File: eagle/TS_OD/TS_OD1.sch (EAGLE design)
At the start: 44 parts, among them IC1 LM4558N, T1 2SC1815, T2 2SC1814

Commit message: change eagle files' name from TS_OD to TS_OD1
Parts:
- C10, C11: device rcl:CPOL-EUE2.5-7 -> rcl:CPOL-EUE5-6
- R7: device rcl:R-EU_0207/7 -> rcl:R-EU_0207/10
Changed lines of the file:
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@@
 <part name="P+4" library="supply1" deviceset="VCC/2" device=""/>
 <part name="JP2" library="pinhead" deviceset="PINHD-1X2" device="" value="DRIVE"/>
-<part name="R7" library="rcl" deviceset="R-EU_" device="0207/7" value="1k"/>
+<part name="R7" library="rcl" deviceset="R-EU_" device="0207/10" value="1k"/>
 <part name="R9" library="rcl" deviceset="R-EU_" device="0207/7" value="10k"/>
 <part name="C5" library="rcl" deviceset="C-EU" device="050-035X075" value="0.22uF"/>
@@
 <part name="R16" library="rcl" deviceset="R-EU_" device="0207/7" value="10k"/>
 <part name="R17" library="rcl" deviceset="R-EU_" device="0207/7" value="10k"/>
-<part name="C10" library="rcl" deviceset="CPOL-EU" device="E2.5-7" value="100uF"/>
-<part name="C11" library="rcl" deviceset="CPOL-EU" device="E2.5-7" value="47uF"/>
+<part name="C10" library="rcl" deviceset="CPOL-EU" device="E5-6" value="100uF"/>
+<part name="C11" library="rcl" deviceset="CPOL-EU" device="E5-6" value="47uF"/>
 <part name="GND9" library="supply1" deviceset="GND" device=""/>
 <part name="P+9" library="supply1" deviceset="VCC/2" device=""/>

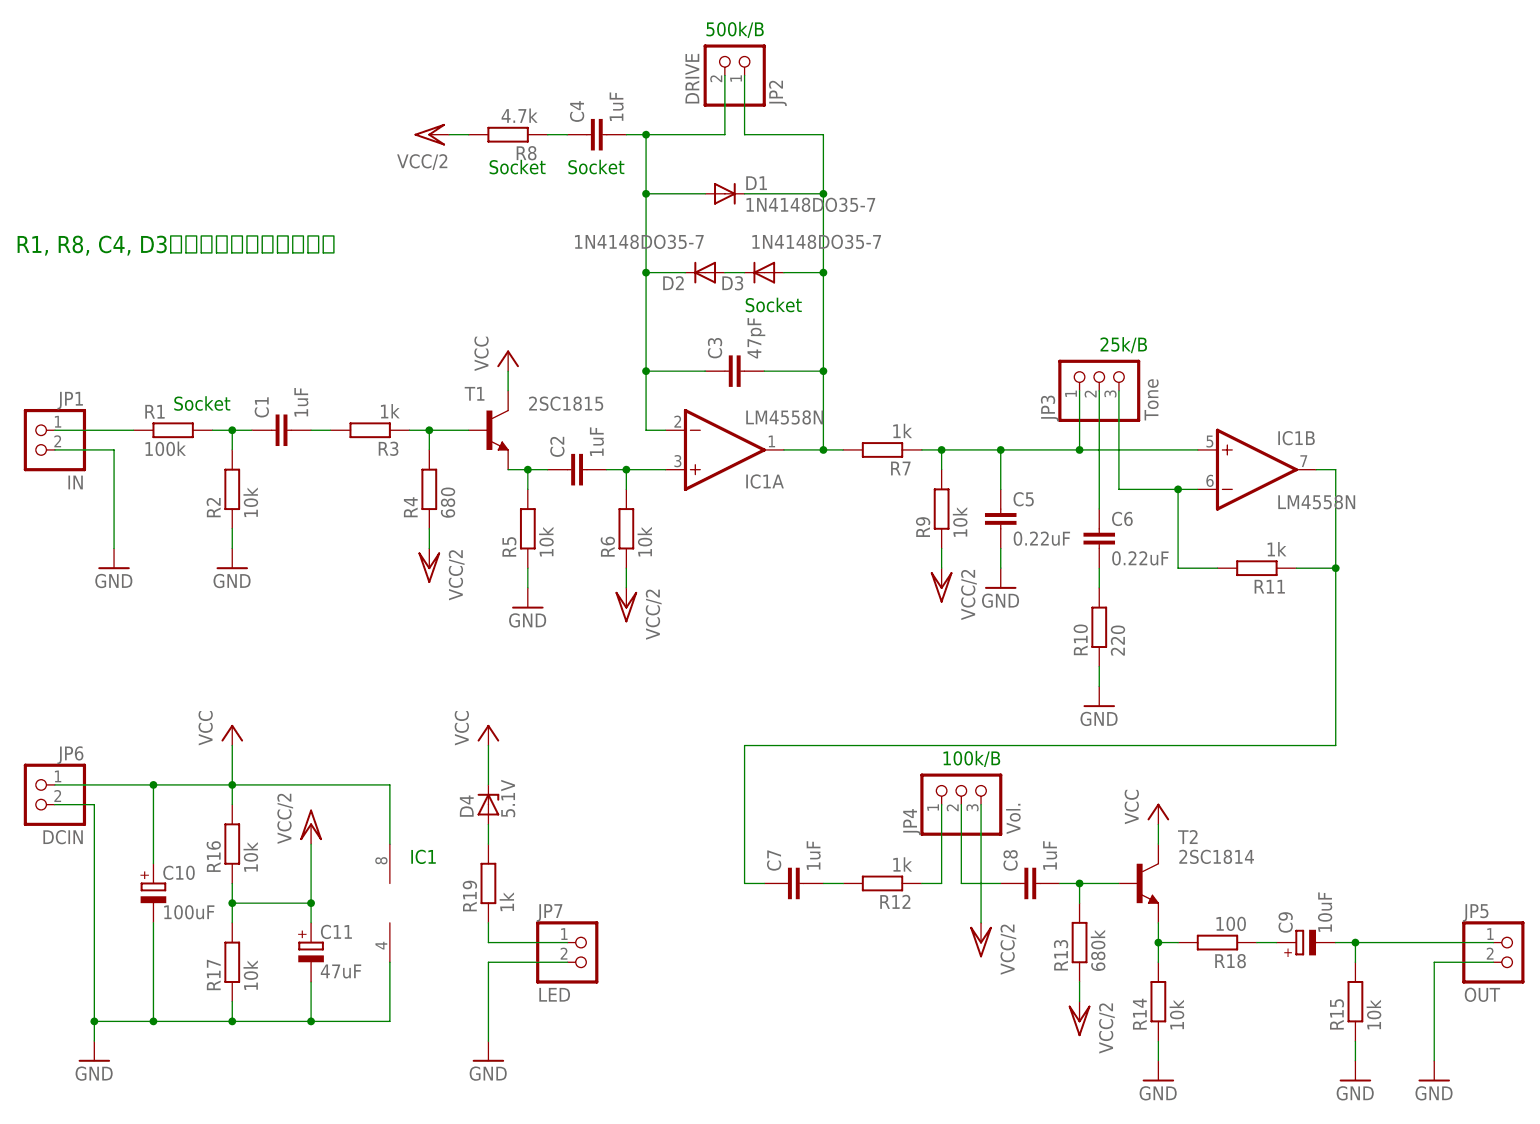
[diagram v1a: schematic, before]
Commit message: Update: eagle files Add: drawing of the case
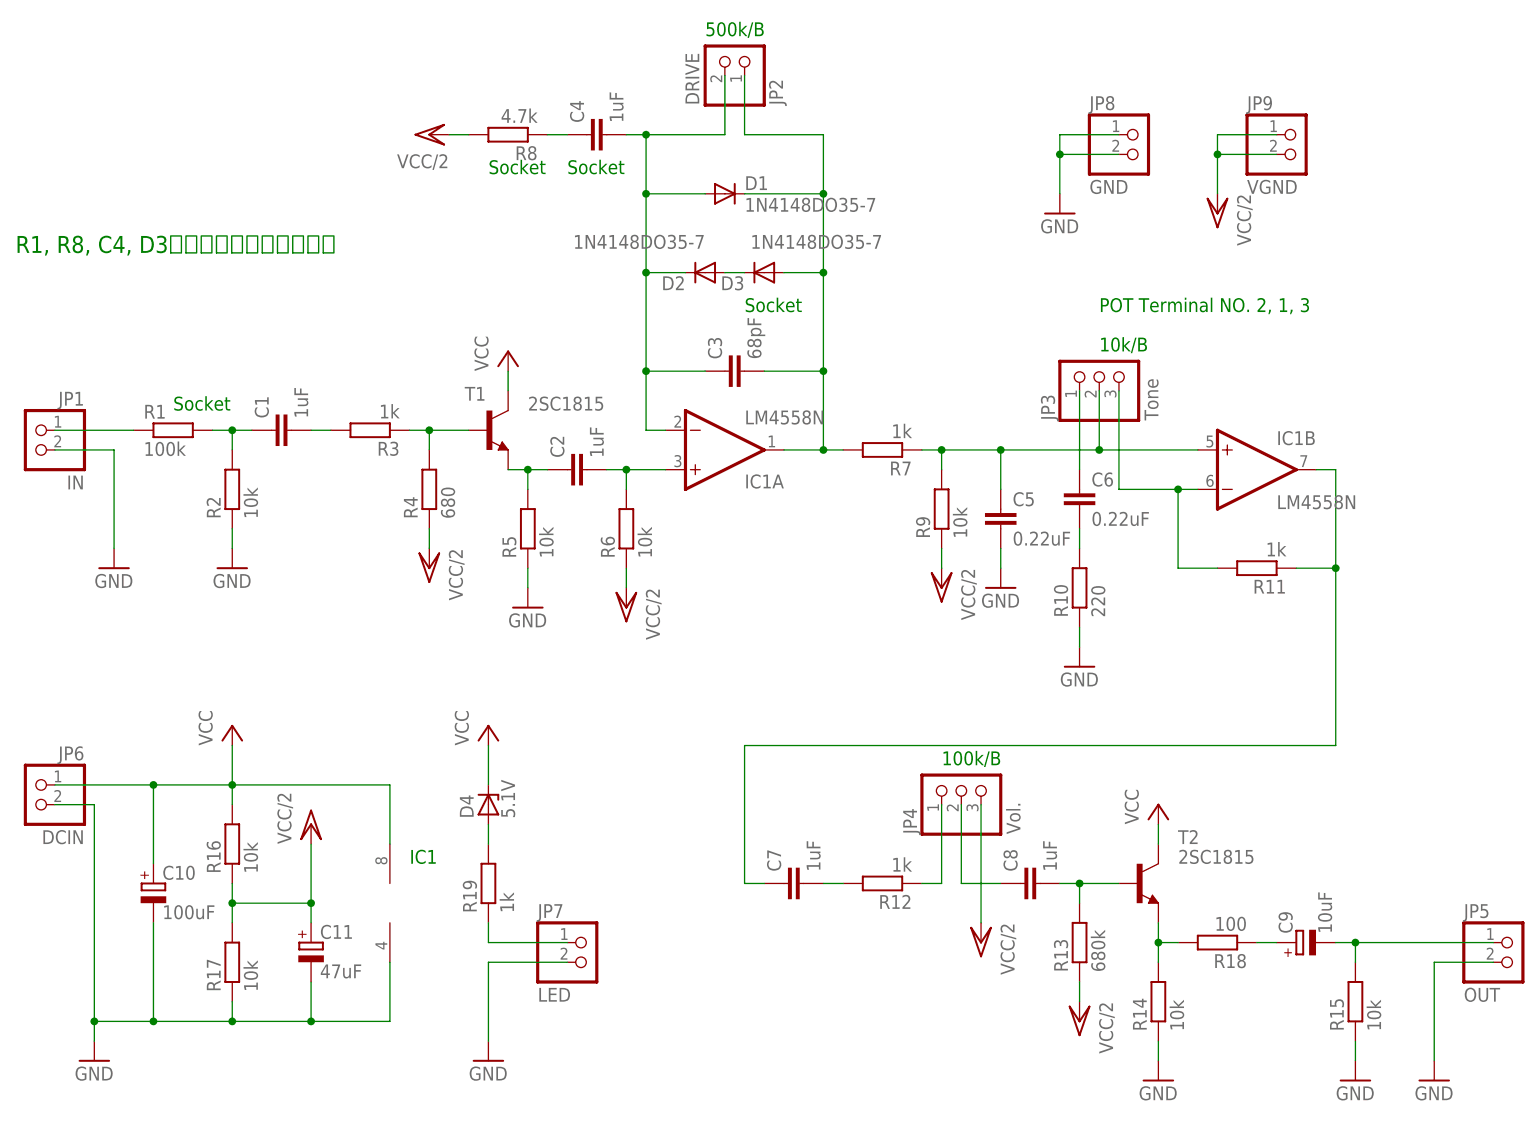
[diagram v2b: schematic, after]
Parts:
- added JP8: GND, pinhead:PINHD-1X2
- added JP9: VGND, pinhead:PINHD-1X2
- C3: value 47pF -> 68pF
- T2: value 2SC1814 -> 2SC1815
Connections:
- net GND: now also JP8.1, JP8.2
- net N$14: now also JP3.1; no longer JP3.2
- net N$4: now also JP3.2; no longer JP3.1
- net VCC/2: now also JP9.1, JP9.2
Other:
- note added: "10k/B"
- note added: "POT Terminal NO. 2, 1, 3"
- note removed: "25k/B"
- moved on the sheet: C6, R10
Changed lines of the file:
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@@
 <part name="P+2" library="supply1" deviceset="VCC/2" device=""/>
 <part name="IC1" library="linear" deviceset="*4558" device="N" technology="LM"/>
-<part name="C3" library="rcl" deviceset="C-EU" device="050-024X044" value="47pF"/>
+<part name="C3" library="rcl" deviceset="C-EU" device="050-024X044" value="68pF"/>
 <part name="D1" library="diode" deviceset="1N4148" device="DO35-7"/>
 <part name="D2" library="diode" deviceset="1N4148" device="DO35-7"/>
@@
 <part name="R13" library="rcl" deviceset="R-EU_" device="0207/7" value="680k"/>
 <part name="P+7" library="supply1" deviceset="VCC/2" device=""/>
-<part name="T2" library="transistor" deviceset="*-NPN-" device="TO92-ECB" value="2SC1814"/>
+<part name="T2" library="transistor" deviceset="*-NPN-" device="TO92-ECB" value="2SC1815"/>
 <part name="P+8" library="supply1" deviceset="VCC" device=""/>
 <part name="R14" library="rcl" deviceset="R-EU_" device="0207/7" value="10k"/>
@@
 <part name="GND10" library="supply1" deviceset="GND" device=""/>
 <part name="JP7" library="pinhead" deviceset="PINHD-1X2" device="" value="LED"/>
+<part name="JP8" library="pinhead" deviceset="PINHD-1X2" device="" value="GND"/>
+<part name="GND11" library="supply1" deviceset="GND" device=""/>
+<part name="JP9" library="pinhead" deviceset="PINHD-1X2" device="" value="VGND"/>
+<part name="P+12" library="supply1" deviceset="VCC/2" device=""/>
 </parts>
 <sheets>
@@
 <text x="88.9" y="149.86" size="1.778" layer="91">Socket</text>
 <text x="121.92" y="132.08" size="1.778" layer="91">Socket</text>
-<text x="167.64" y="127" size="1.778" layer="91">25k/B</text>
+<text x="167.64" y="127" size="1.778" layer="91">10k/B</text>
 <text x="147.32" y="73.66" size="1.778" layer="91">100k/B</text>
 <text x="27.94" y="139.7" size="2.1844" layer="91">R1, R8, C4, D3はピン・ソケットで実装</text>
 <text x="78.74" y="60.96" size="1.778" layer="91">IC1</text>
 <text x="99.06" y="149.86" size="1.778" layer="91">Socket</text>
+<text x="167.64" y="132.08" size="1.778" layer="91">POT Terminal NO. 2, 1, 3</text>
 </plain>
 <instances>
@@
 <instance part="IC1" gate="B" x="187.96" y="111.76"/>
 <instance part="JP3" gate="A" x="167.64" y="124.46" rot="R90"/>
-<instance part="C6" gate="G$1" x="167.64" y="104.14"/>
-<instance part="R10" gate="G$1" x="167.64" y="91.44" rot="R90"/>
+<instance part="C6" gate="G$1" x="165.1" y="109.22"/>
+<instance part="R10" gate="G$1" x="165.1" y="96.52" rot="R90"/>
 <instance part="P+5" gate="G$1" x="147.32" y="96.52" rot="R180"/>
 <instance part="GND4" gate="1" x="154.94" y="96.52"/>
-<instance part="GND5" gate="1" x="167.64" y="81.28"/>
+<instance part="GND5" gate="1" x="165.1" y="86.36"/>
 <instance part="R11" gate="G$1" x="187.96" y="99.06" rot="R180"/>
 <instance part="C7" gate="G$1" x="127" y="58.42" rot="R90"/>
@@
 <instance part="GND10" gate="1" x="88.9" y="35.56"/>
 <instance part="JP7" gate="G$1" x="101.6" y="48.26"/>
+<instance part="JP8" gate="G$1" x="172.72" y="152.4"/>
+<instance part="GND11" gate="1" x="162.56" y="144.78"/>
+<instance part="JP9" gate="G$1" x="193.04" y="152.4"/>
+<instance part="P+12" gate="G$1" x="182.88" y="144.78" rot="R180"/>
 </instances>
 <busses>
@@
 <pinref part="GND5" gate="1" pin="GND"/>
 <pinref part="R10" gate="G$1" pin="1"/>
-<wire x1="167.64" y1="83.82" x2="167.64" y2="86.36" width="0.1524" layer="91"/>
+<wire x1="165.1" y1="88.9" x2="165.1" y2="91.44" width="0.1524" layer="91"/>
 </segment>
 <segment>
@@
 <wire x1="88.9" y1="48.26" x2="88.9" y2="38.1" width="0.1524" layer="91"/>
 </segment>
+<segment>
+<pinref part="JP8" gate="G$1" pin="1"/>
+<wire x1="170.18" y1="154.94" x2="162.56" y2="154.94" width="0.1524" layer="91"/>
+<wire x1="162.56" y1="154.94" x2="162.56" y2="152.4" width="0.1524" layer="91"/>
+<pinref part="JP8" gate="G$1" pin="2"/>
+<wire x1="162.56" y1="152.4" x2="162.56" y2="147.32" width="0.1524" layer="91"/>
+<wire x1="170.18" y1="152.4" x2="162.56" y2="152.4" width="0.1524" layer="91"/>
+<junction x="162.56" y="152.4"/>
+<pinref part="GND11" gate="1" pin="GND"/>
+</segment>
 </net>
 <net name="N$5" class="0">
@@
 <wire x1="66.04" y1="63.5" x2="66.04" y2="55.88" width="0.1524" layer="91"/>
 <junction x="66.04" y="55.88"/>
+</segment>
+<segment>
+<pinref part="JP9" gate="G$1" pin="1"/>
+<wire x1="190.5" y1="154.94" x2="182.88" y2="154.94" width="0.1524" layer="91"/>
+<pinref part="P+12" gate="G$1" pin="VCC/2"/>
+<wire x1="182.88" y1="154.94" x2="182.88" y2="152.4" width="0.1524" layer="91"/>
+<pinref part="JP9" gate="G$1" pin="2"/>
+<wire x1="182.88" y1="152.4" x2="182.88" y2="147.32" width="0.1524" layer="91"/>
+<wire x1="182.88" y1="152.4" x2="190.5" y2="152.4" width="0.1524" layer="91"/>
+<junction x="182.88" y="152.4"/>
 </segment>
 </net>
@@
 <pinref part="C5" gate="G$1" pin="1"/>
 <wire x1="154.94" y1="114.3" x2="154.94" y2="109.22" width="0.1524" layer="91"/>
-<wire x1="154.94" y1="114.3" x2="165.1" y2="114.3" width="0.1524" layer="91"/>
 <junction x="154.94" y="114.3"/>
-<pinref part="JP3" gate="A" pin="1"/>
-<wire x1="165.1" y1="114.3" x2="165.1" y2="121.92" width="0.1524" layer="91"/>
 <pinref part="IC1" gate="B" pin="+IN"/>
-<wire x1="165.1" y1="114.3" x2="180.34" y2="114.3" width="0.1524" layer="91"/>
-<junction x="165.1" y="114.3"/>
+<wire x1="154.94" y1="114.3" x2="167.64" y2="114.3" width="0.1524" layer="91"/>
+<pinref part="JP3" gate="A" pin="2"/>
+<wire x1="167.64" y1="114.3" x2="180.34" y2="114.3" width="0.1524" layer="91"/>
+<wire x1="167.64" y1="121.92" x2="167.64" y2="114.3" width="0.1524" layer="91"/>
+<junction x="167.64" y="114.3"/>
 </segment>
 </net>
@@
 <pinref part="R10" gate="G$1" pin="2"/>
 <pinref part="C6" gate="G$1" pin="2"/>
-<wire x1="167.64" y1="96.52" x2="167.64" y2="99.06" width="0.1524" layer="91"/>
-</segment>
-</net>
-<net name="N$14" class="0">
-<segment>
-<pinref part="C6" gate="G$1" pin="1"/>
-<pinref part="JP3" gate="A" pin="2"/>
-<wire x1="167.64" y1="106.68" x2="167.64" y2="121.92" width="0.1524" layer="91"/>
+<wire x1="165.1" y1="101.6" x2="165.1" y2="104.14" width="0.1524" layer="91"/>
 </segment>
 </net>
@@
 </segment>
 </net>
+<net name="N$14" class="0">
+<segment>
+<pinref part="JP3" gate="A" pin="1"/>
+<pinref part="C6" gate="G$1" pin="1"/>
+<wire x1="165.1" y1="121.92" x2="165.1" y2="111.76" width="0.1524" layer="91"/>
+</segment>
+</net>
